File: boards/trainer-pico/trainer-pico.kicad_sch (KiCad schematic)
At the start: 36 parts, among them J1 Conn_01x08_Pin, J10 Conn_01x04_Socket, J11 Conn_01x17_Pin, J12 Conn_01x17_Socket, J13 Conn_01x17_Socket, J14 Conn_01x17_Pin, J15 Barrel_Jack_Switch, J16 Conn_01x04_Pin, J17 Conn_01x04_Pin, J18 Conn_01x04_Pin, J2 Conn_01x04_Pin, J3 Conn_01x06_Pin, J4 Conn_01x04_Pin, J5 Conn_01x04_Pin, J6 Conn_01x08_Socket, J7 Conn_01x04_Socket, J8 Conn_01x06_Socket, J9 Conn_01x04_Socket, U2 L7805, U3 L7809

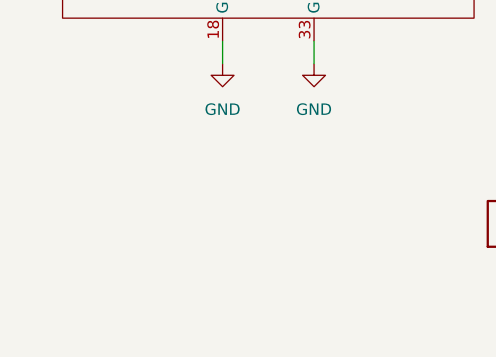
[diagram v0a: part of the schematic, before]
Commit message: 電源のテストポイントを追加
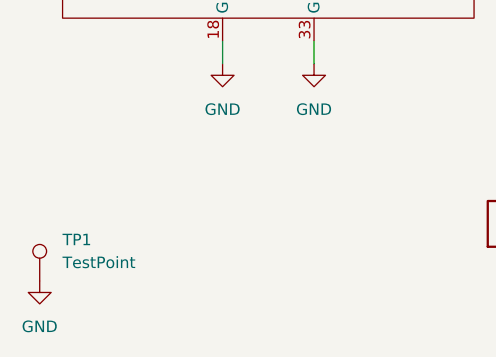
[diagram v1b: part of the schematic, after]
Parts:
- added TP1: TestPoint, Connector_PinHeader_2.54mm:PinHeader_1x01_P2.54mm_Vertical, symbol Connector:TestPoint
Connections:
- net GND: now also TP1.1

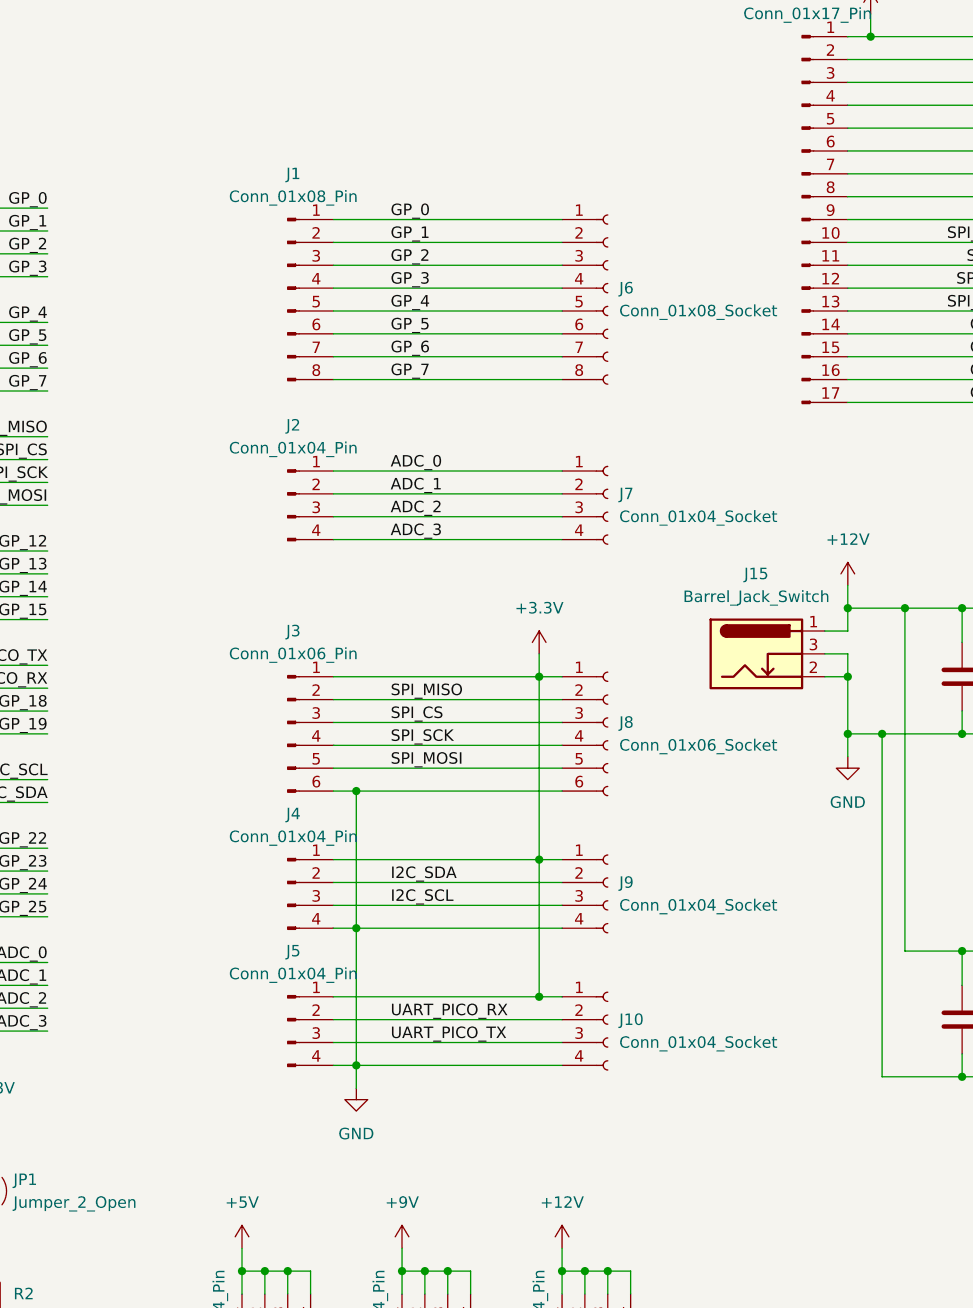
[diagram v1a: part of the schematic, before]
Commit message: 不要なシンボルの削除
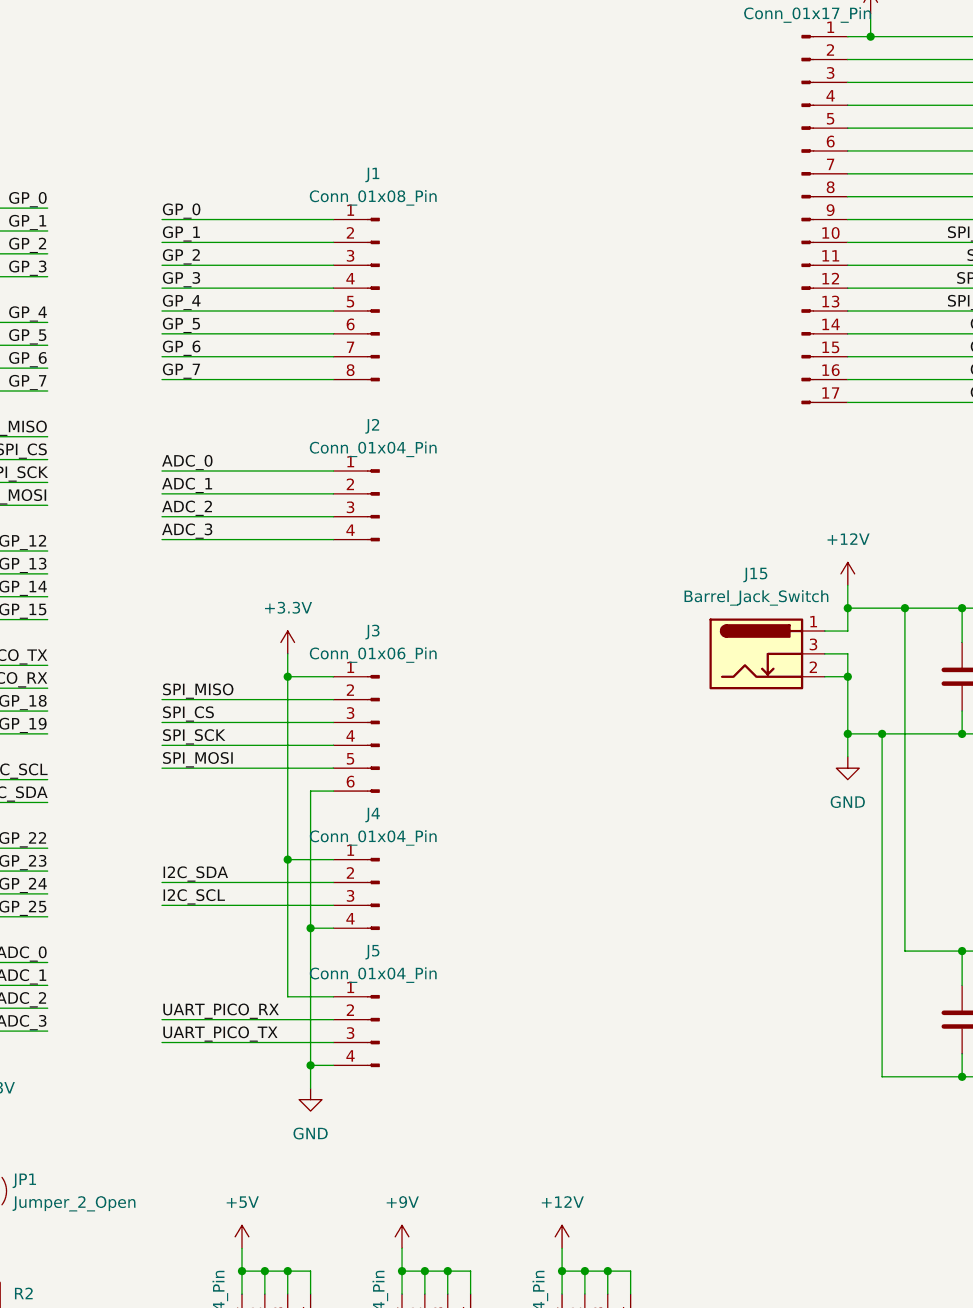
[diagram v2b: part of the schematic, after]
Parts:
- removed J10, J7, J9: Conn_01x04_Socket, Connector_PinSocket_2.54mm:PinSocket_1x04_P2.54mm_Vertical, symbol Connector:Conn_01x04_Socket
- removed J6: Conn_01x08_Socket, Connector_PinSocket_2.54mm:PinSocket_1x08_P2.54mm_Vertical, symbol Connector:Conn_01x08_Socket
- removed J8: Conn_01x06_Socket, Connector_PinSocket_2.54mm:PinSocket_1x06_P2.54mm_Vertical, symbol Connector:Conn_01x06_Socket
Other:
- moved on the sheet: J1, J2, J3, J4, J5

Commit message: 回路の更新と、AW の修正
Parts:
- removed J16, J17, J18: Conn_01x04_Pin, Connector_PinSocket_2.54mm:PinSocket_1x04_P2.54mm_Vertical, symbol Connector:Conn_01x04_Pin
- added J6: Conn_02x15_Odd_Even, Connector_PinSocket_2.54mm:PinSocket_2x15_P2.54mm_Horizontal, symbol Connector_Generic:Conn_02x15_Odd_Even
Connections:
- net +12V: now also J6.29 (Pin_29), J6.30 (Pin_30)
- net +3.3V: now also J6.23 (Pin_23), J6.24 (Pin_24)
- net +5V: now also J6.25 (Pin_25), J6.26 (Pin_26)
- net +9V: now also J6.27 (Pin_27), J6.28 (Pin_28)
- net ADC_0: now also J6.18 (Pin_18)
- net ADC_1: now also J6.17 (Pin_17)
- net ADC_2: now also J6.20 (Pin_20)
- net ADC_3: now also J6.19 (Pin_19)
- net GND: now also J6.21 (Pin_21), J6.22 (Pin_22)
- net GP_0: now also J6.10 (Pin_10)
- net GP_1: now also J6.9 (Pin_9)
- net GP_2: now also J6.12 (Pin_12)
- net GP_3: now also J6.11 (Pin_11)
- net GP_4: now also J6.14 (Pin_14)
- net GP_5: now also J6.13 (Pin_13)
- net GP_6: now also J6.16 (Pin_16)
- net GP_7: now also J6.15 (Pin_15)
- net I2C_SCL: now also J6.1 (Pin_1)
- net I2C_SDA: now also J6.3 (Pin_3)
- net SPI_CS: now also J6.8 (Pin_8)
- net SPI_MISO: now also J6.7 (Pin_7)
- net SPI_MOSI: now also J6.6 (Pin_6)
- net SPI_SCK: now also J6.5 (Pin_5)
- net UART_PICO_RX: now also J6.4 (Pin_4)
- net UART_PICO_TX: now also J6.2 (Pin_2)

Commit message: ピン配変更
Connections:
- net SPI_CS: now also J6.7 (Pin_7); no longer J6.8 (Pin_8)
- net SPI_MISO: now also J6.8 (Pin_8); no longer J6.7 (Pin_7)

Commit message: test point を TH にした
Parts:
- added TP2, TP3, TP4: TestPoint, Connector_PinHeader_2.54mm:PinHeader_1x01_P2.54mm_Vertical, symbol Connector:TestPoint
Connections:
- net +12V: now also TP4.1
- net +5V: now also TP2.1
- net +9V: now also TP3.1
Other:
- moved on the sheet: TP1
